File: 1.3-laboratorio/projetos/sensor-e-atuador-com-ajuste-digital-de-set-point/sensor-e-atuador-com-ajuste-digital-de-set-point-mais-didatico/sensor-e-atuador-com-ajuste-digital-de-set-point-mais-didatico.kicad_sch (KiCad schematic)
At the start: 50 parts, among them J1 Conn_01x02, J2 Conn_01x01, J3 Conn_01x01, P1 47k, P2 47k, SW1 SW_PUSH, U1 LM324N, U2 4093, U3 4518, U4 CD4511BE, U5 SM42056-1

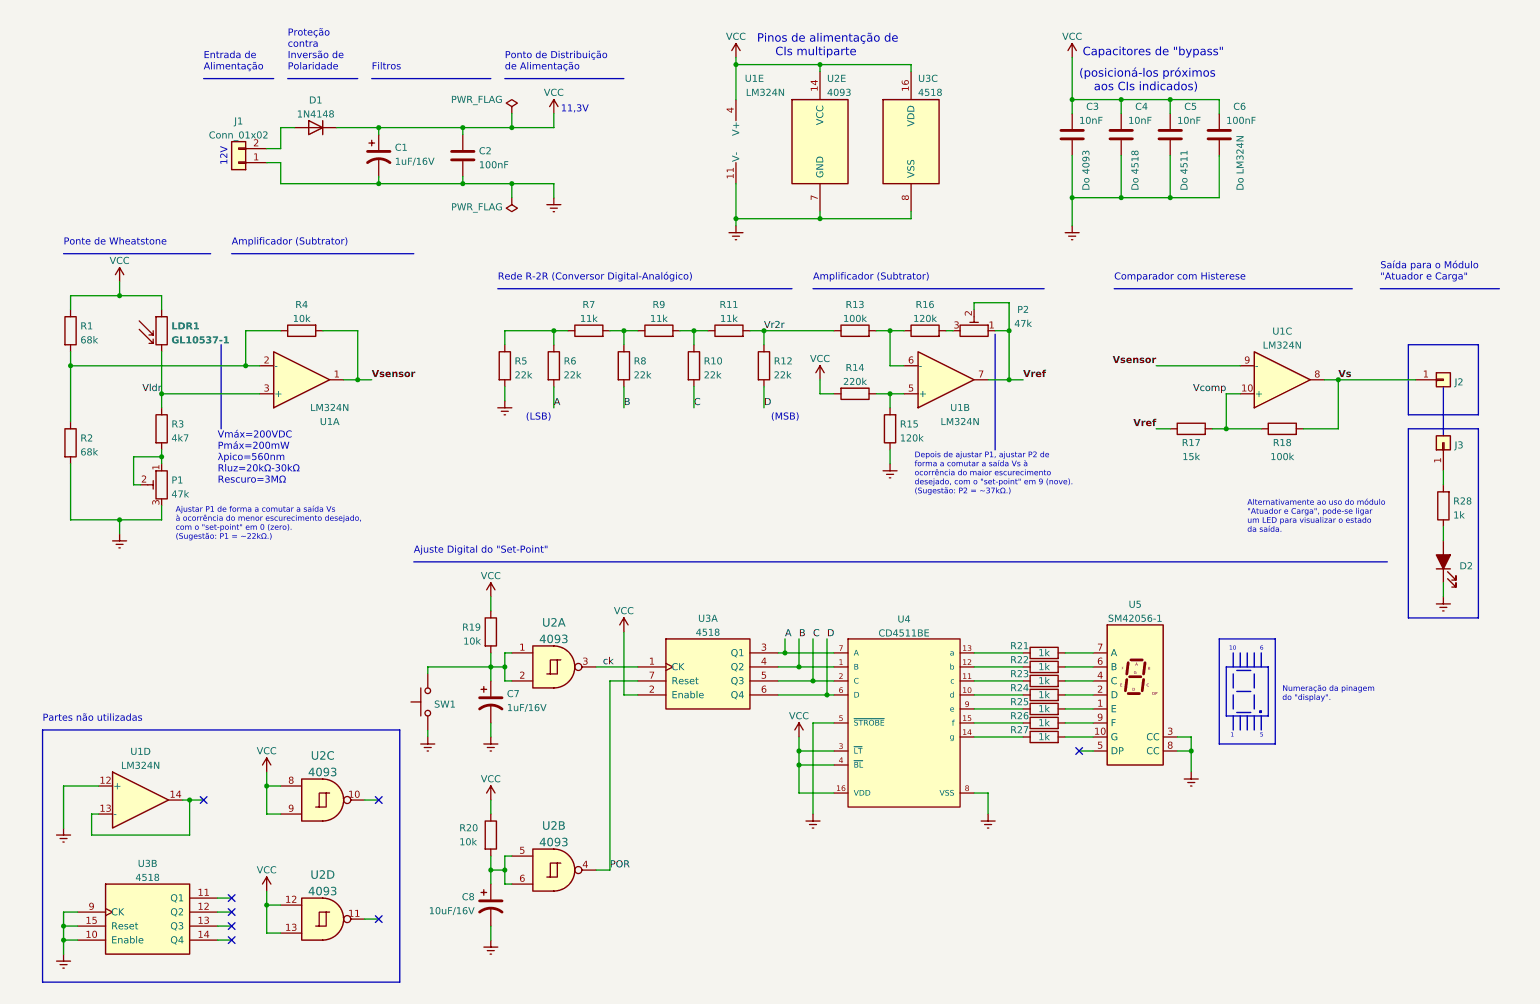
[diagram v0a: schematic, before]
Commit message: Edição da versão didática v. 1.0.0, incluindo informações para depuração, concluída.
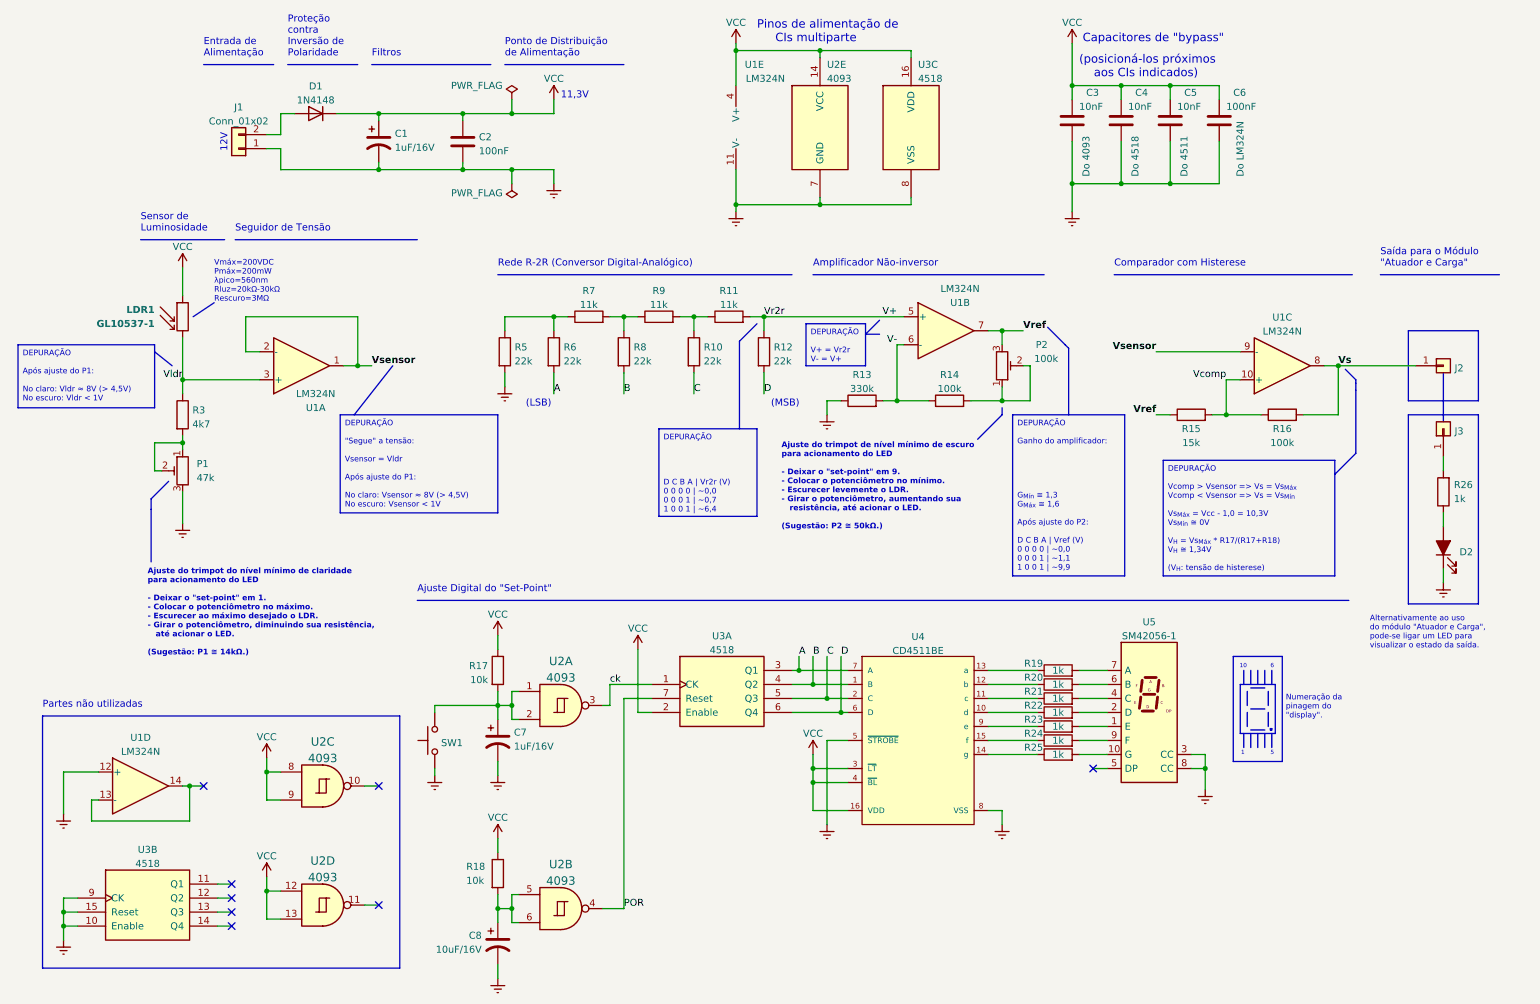
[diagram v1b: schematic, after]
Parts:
- removed R1, R2: 68k, symbol Device:R
- removed R14: 220k, symbol Device:R
- removed R15: 120k, symbol Device:R
- removed R4: 10k, symbol Device:R
- P2: value 47k -> 100k
- R13: renamed from R16; value 120k -> 330k
- renumbered R13 to R14, R17 to R15, R18 to R16, R19 to R17, R20 to R18, R21 to R19, R22 to R20, R23 to R21, R24 to R22, R25 to R23, R26 to R24, R27 to R25, R28 to R26
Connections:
- net Earth: now also R13.1
- net Vref: now also P2.3; no longer P2.1, P2.2
- net Vsensor: now also U1.2 (-)
- net V+: now reaches U1.5 (+)
- net V+: now also R11.2, R12.1
- net V-: now reaches R13.2
- net V-: now also R14.1, U1.6 (-); no longer P2.3
- removed net Vr2r: R11.2, R12.1, R14.1
- new net: P2.1, P2.2, R14.2
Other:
- note added: "Ajuste do trimpot de nível mínimo de escuro para acionamento do LED - Deixar o "set-point" em 9. - Colocar o potenciômetro no mínimo. - Escurecer levemente o LDR. - Girar o potenciômetro, aumentando sua resistência, até acionar o LED. (Sugestão: P2 ≅ 50kΩ.)"
- note added: "Ajuste do trimpot do nível mínimo de claridade para acionamento do LED - Deixar o "set-point" em 1. - Colocar o potenciômetro no máximo. - Escurecer ao máximo desejado o LDR. - Girar o potenciômetro, diminuindo sua resistência, até acionar o LED. (Sugestão: P1 ≅ 14kΩ.)"
- note added: "Amplificador Não-inversor"
- note added: "Seguidor de Tensão"
- note added: "Sensor de Luminosidade"
- note removed: "Ajustar P1 de forma a comutar a saída Vs à ocorrência do menor escurecimento desejado, com o "set-point" em 0 (zero). (Sugestão: P1 = ~22kΩ.)"
- note removed: "Amplificador (Subtrator)"
- note removed: "Depois de ajustar P1, ajustar P2 de forma a comutar a saída Vs à ocorrência do maior escurecimento desejado, com o "set-point" em 9 (nove). (Sugestão: P2 = ~37kΩ.)"
- note removed: "Ponte de Wheatstone"
- moved on the sheet: C1, C2, C3, C4, C5, C6, C7, C8, D1, D2, J1, J2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

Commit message: Ajustes no esquema elétrico conforme ensaio realizado em protoboard. ERC realizado. Alguns componentes da biblioteca 'power' precisaram ser 'reatribuídos' à própria definição para o ERC encontrá-lo nesta biblioteca.
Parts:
- P1: value 47k -> 50k
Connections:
- net POR: now also U2.11; no longer U2.4
- net V+: now also U1.10 (+); no longer U1.5 (+)
- net V-: now also U1.9 (-); no longer U1.6 (-)
- net VCC: now also U2.5, U2.6; no longer U2.12, U2.13
- net Vcomp: now also U1.5 (+); no longer U1.10 (+)
- net Vref: now also U1.8; no longer U1.7
- net Vs: now also U1.7; no longer U1.8
- net Vsensor: now also U1.6 (-); no longer U1.9 (-)
- net at C8.1, R18.2: now also U2.12, U2.13; no longer U2.5, U2.6
- no-connect marks 8 -> 7
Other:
- note added: "Ajuste do trimpot (P1) do nível mínimo de claridade para acionamento do LED - Deixar o "set-point" em 1. - Colocar o trimpot no máximo. - Escurecer ao máximo desejado o LDR. - Girar o trimpot, diminuindo sua resistência: # até acionar o LED; ou, alternativamente, # até obter Vldr ≈ 10V. (Sugestão: P1 ≅ 14kΩ.)"
- note added: "Ajuste do trimpot (P2) de nível mínimo de escuro para acionamento do LED - Deixar o "set-point" em 9. - Colocar o trimpot no mínimo. - Escurecer levemente o LDR. - Girar o trimpot, aumentando sua resistência: # até acionar o LED; ou, alternativamente, # até obter Vref ≈ 9,9V. (Sugestão: P2 ≅ 75kΩ.)"
- note added: "Alternativamente ao uso do módulo "Atuador e Carga", pode-se ligar o LED acima para visualizar o estado da saída."
- note removed: "Ajuste do trimpot de nível mínimo de escuro para acionamento do LED - Deixar o "set-point" em 9. - Colocar o potenciômetro no mínimo. - Escurecer levemente o LDR. - Girar o potenciômetro, aumentando sua resistência, até acionar o LED. (Sugestão: P2 ≅ 50kΩ.)"
- note removed: "Ajuste do trimpot do nível mínimo de claridade para acionamento do LED - Deixar o "set-point" em 1. - Colocar o potenciômetro no máximo. - Escurecer ao máximo desejado o LDR. - Girar o potenciômetro, diminuindo sua resistência, até acionar o LED. (Sugestão: P1 ≅ 14kΩ.)"
- note removed: "Alternativamente ao uso do módulo "Atuador e Carga", pode-se ligar um LED para visualizar o estado da saída."

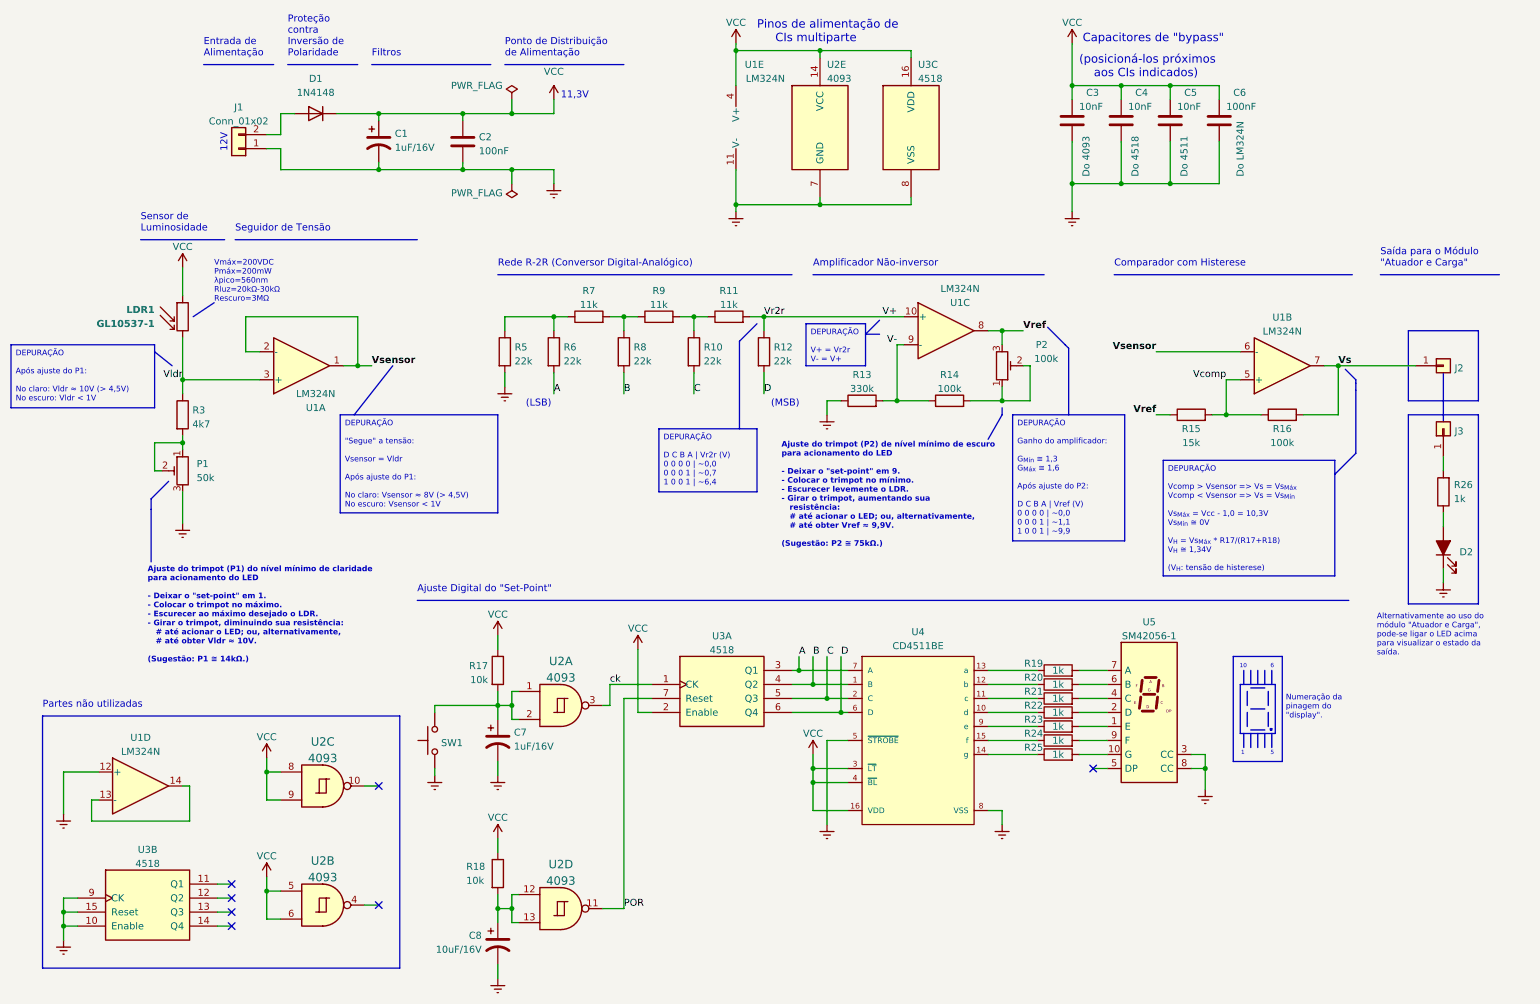
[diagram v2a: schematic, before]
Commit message: Ajustes feitos no esquema elétrico.
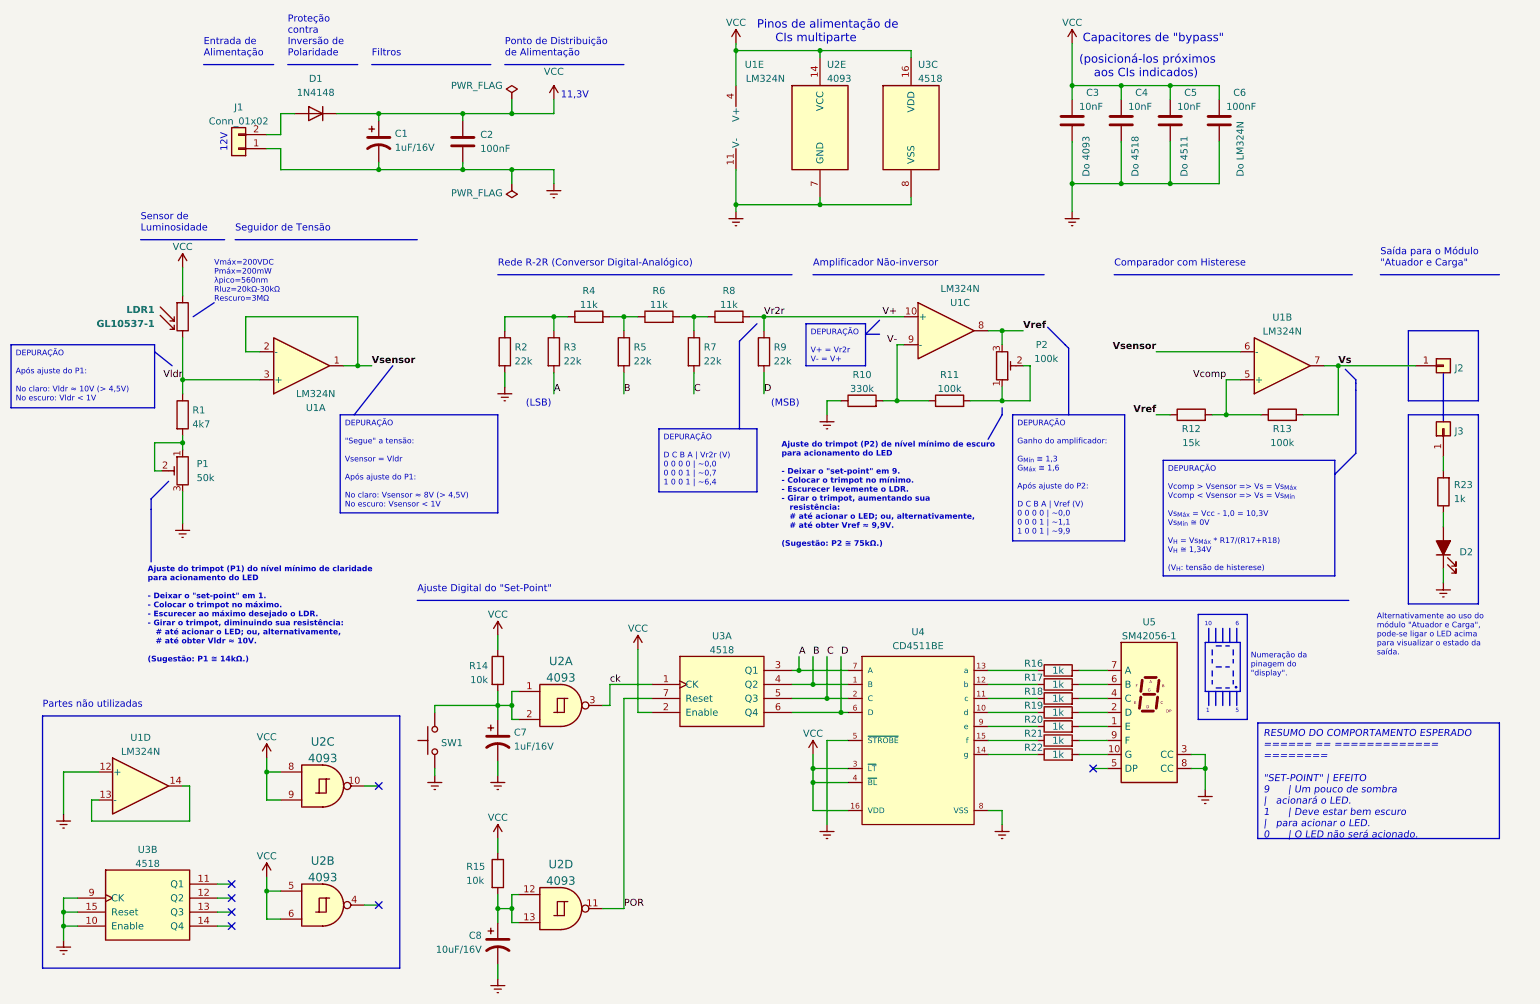
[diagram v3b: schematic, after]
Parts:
- C1: footprint (none) -> Capacitor_THT:CP_Radial_D5.0mm_P2.50mm
- C2: footprint (none) -> Capacitor_THT:C_Disc_D6.0mm_W2.5mm_P5.00mm
- C3, C4, C5: footprint Capacitor_THT:C_Disc_D5.0mm_W2.5mm_P2.50mm -> Capacitor_THT:C_Disc_D5.0mm_W2.5mm_P5.00mm
- C6: footprint Capacitor_THT:C_Disc_D5.0mm_W2.5mm_P2.50mm -> Capacitor_THT:C_Disc_D6.0mm_W2.5mm_P5.00mm
- D2: footprint (none) -> LED_THT:LED_D3.0mm
- J1: footprint (none) -> TerminalBlock_Phoenix:TerminalBlock_Phoenix_MKDS-1,5-2-5.08_1x02_P5.08mm_Horizontal
- J2, J3: footprint (none) -> Connector_PinHeader_1.00mm:PinHeader_1x01_P1.00mm_Vertical
- LDR1: footprint (none) -> OptoDevice:R_LDR_10x8.5mm_P7.6mm_Vertical
- P1, P2: footprint (none) -> Potentiometer_THT:Potentiometer_ACP_CA9-H5_Horizontal
- R1: renamed from R3; footprint (none) -> Resistor_THT:R_Axial_DIN0207_L6.3mm_D2.5mm_P7.62mm_Horizontal
- R10: renamed from R13; footprint (none) -> Resistor_THT:R_Axial_DIN0207_L6.3mm_D2.5mm_P7.62mm_Horizontal
- R11: renamed from R14; footprint (none) -> Resistor_THT:R_Axial_DIN0207_L6.3mm_D2.5mm_P7.62mm_Horizontal
- R12: renamed from R15; footprint (none) -> Resistor_THT:R_Axial_DIN0207_L6.3mm_D2.5mm_P7.62mm_Horizontal
- R13: renamed from R16; footprint (none) -> Resistor_THT:R_Axial_DIN0207_L6.3mm_D2.5mm_P7.62mm_Horizontal
- R14: renamed from R17; footprint Resistor_THT:R_Axial_DIN0207_L6.3mm_D2.5mm_P10.16mm_Horizontal -> Resistor_THT:R_Axial_DIN0207_L6.3mm_D2.5mm_P7.62mm_Horizontal
- R15: renamed from R18; footprint Resistor_THT:R_Axial_DIN0207_L6.3mm_D2.5mm_P10.16mm_Horizontal -> Resistor_THT:R_Axial_DIN0207_L6.3mm_D2.5mm_P7.62mm_Horizontal
- R16: renamed from R19; footprint Resistor_THT:R_Axial_DIN0207_L6.3mm_D2.5mm_P10.16mm_Horizontal -> Resistor_THT:R_Axial_DIN0207_L6.3mm_D2.5mm_P7.62mm_Horizontal
- R17: renamed from R20; footprint Resistor_THT:R_Axial_DIN0207_L6.3mm_D2.5mm_P10.16mm_Horizontal -> Resistor_THT:R_Axial_DIN0207_L6.3mm_D2.5mm_P7.62mm_Horizontal
- R18: renamed from R21; footprint Resistor_THT:R_Axial_DIN0207_L6.3mm_D2.5mm_P10.16mm_Horizontal -> Resistor_THT:R_Axial_DIN0207_L6.3mm_D2.5mm_P7.62mm_Horizontal
- R19: renamed from R22; footprint Resistor_THT:R_Axial_DIN0207_L6.3mm_D2.5mm_P10.16mm_Horizontal -> Resistor_THT:R_Axial_DIN0207_L6.3mm_D2.5mm_P7.62mm_Horizontal
- R2: renamed from R5; footprint (none) -> Resistor_THT:R_Axial_DIN0207_L6.3mm_D2.5mm_P7.62mm_Horizontal
- R20: renamed from R23; footprint Resistor_THT:R_Axial_DIN0207_L6.3mm_D2.5mm_P10.16mm_Horizontal -> Resistor_THT:R_Axial_DIN0207_L6.3mm_D2.5mm_P7.62mm_Horizontal
- R21: renamed from R24; footprint Resistor_THT:R_Axial_DIN0207_L6.3mm_D2.5mm_P10.16mm_Horizontal -> Resistor_THT:R_Axial_DIN0207_L6.3mm_D2.5mm_P7.62mm_Horizontal
- R22: renamed from R25; footprint Resistor_THT:R_Axial_DIN0207_L6.3mm_D2.5mm_P10.16mm_Horizontal -> Resistor_THT:R_Axial_DIN0207_L6.3mm_D2.5mm_P7.62mm_Horizontal
- R23: renamed from R26; footprint (none) -> Resistor_THT:R_Axial_DIN0207_L6.3mm_D2.5mm_P7.62mm_Horizontal
- R3: renamed from R6; footprint (none) -> Resistor_THT:R_Axial_DIN0207_L6.3mm_D2.5mm_P7.62mm_Horizontal
- R4: renamed from R7; footprint (none) -> Resistor_THT:R_Axial_DIN0207_L6.3mm_D2.5mm_P7.62mm_Horizontal
- R5: renamed from R8; footprint (none) -> Resistor_THT:R_Axial_DIN0207_L6.3mm_D2.5mm_P7.62mm_Horizontal
- R6: renamed from R9; footprint (none) -> Resistor_THT:R_Axial_DIN0207_L6.3mm_D2.5mm_P7.62mm_Horizontal
- R7: renamed from R10; footprint (none) -> Resistor_THT:R_Axial_DIN0207_L6.3mm_D2.5mm_P7.62mm_Horizontal
- R8: renamed from R11; footprint (none) -> Resistor_THT:R_Axial_DIN0207_L6.3mm_D2.5mm_P7.62mm_Horizontal
- R9: renamed from R12; footprint (none) -> Resistor_THT:R_Axial_DIN0207_L6.3mm_D2.5mm_P7.62mm_Horizontal
- U1: footprint (none) -> Package_DIP:DIP-14_W7.62mm_Socket_LongPads
- U2: footprint Package_DIP:DIP-14_W7.62mm_LongPads -> Package_DIP:DIP-14_W7.62mm_Socket_LongPads
- U3: footprint Package_DIP:DIP-16_W7.62mm_LongPads -> Package_DIP:DIP-16_W7.62mm_Socket_LongPads
- U4: footprint Texas_Instruments-CD4511BE-* -> Package_DIP:DIP-16_W7.62mm_Socket_LongPads
- U5: footprint Display_7Segment:KCSC02-105 -> Display_7Segment:HDSP-A151
